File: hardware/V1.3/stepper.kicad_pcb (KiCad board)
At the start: 4 copper layers, 40 x 40 mm, 119 parts, among them J101 USB-MINI-B-SMD, J102 DRILL, J103 DRILL, J104 DRILL, J105 DRILL, J401 STACK-UP-HIGH, J402 STACK-DOWN, J403 STACK-UP-HIGH, J404 STACK-DOWN, P201 black, P202 green, P301 CON-SENSOR, P302 CON-SENSOR, Q201 FDS8449, Q202 AO4421, Q203 2N7002, SW101 Reset, SW102 Erase, U101 AT91SAM3SXB, U102 82400152, U201 ZXCT1086, U202 TMC21XX, U501 LD1117, X101 16Mhz

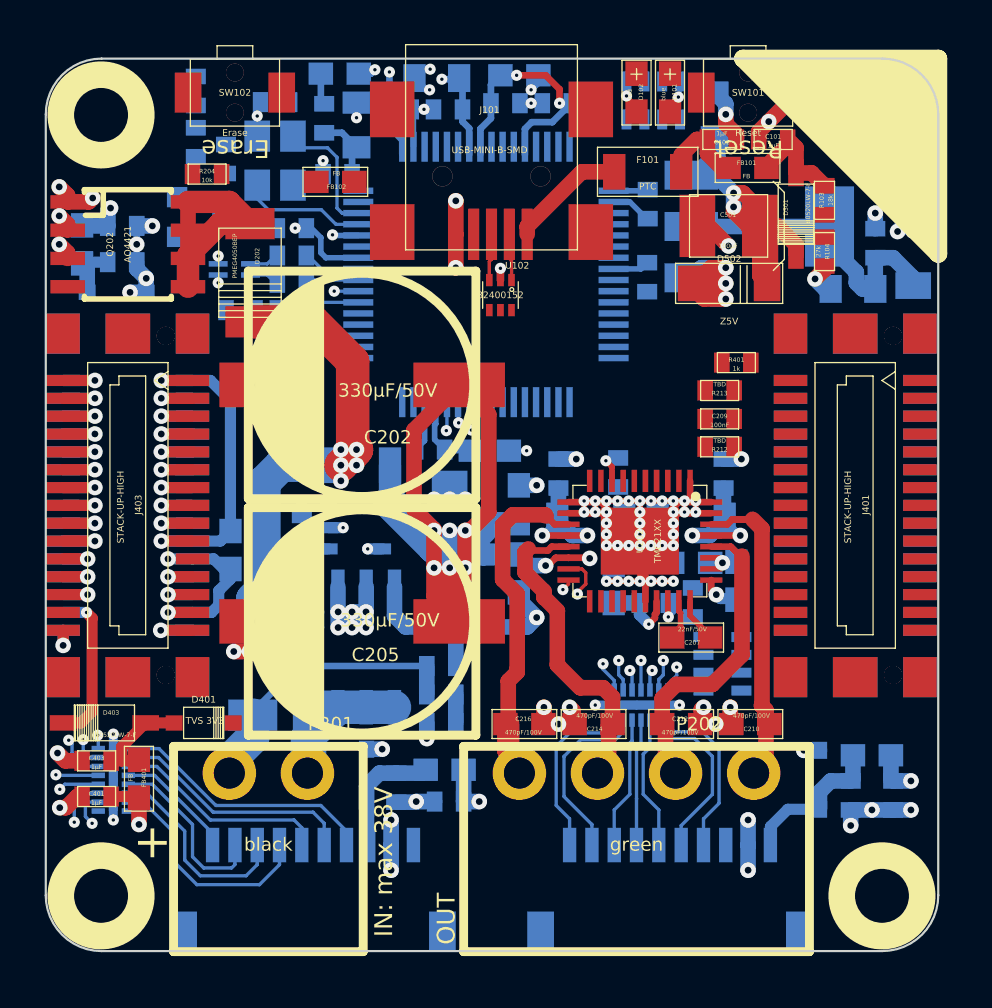
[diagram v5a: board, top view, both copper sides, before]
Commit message: routable, no drc errors
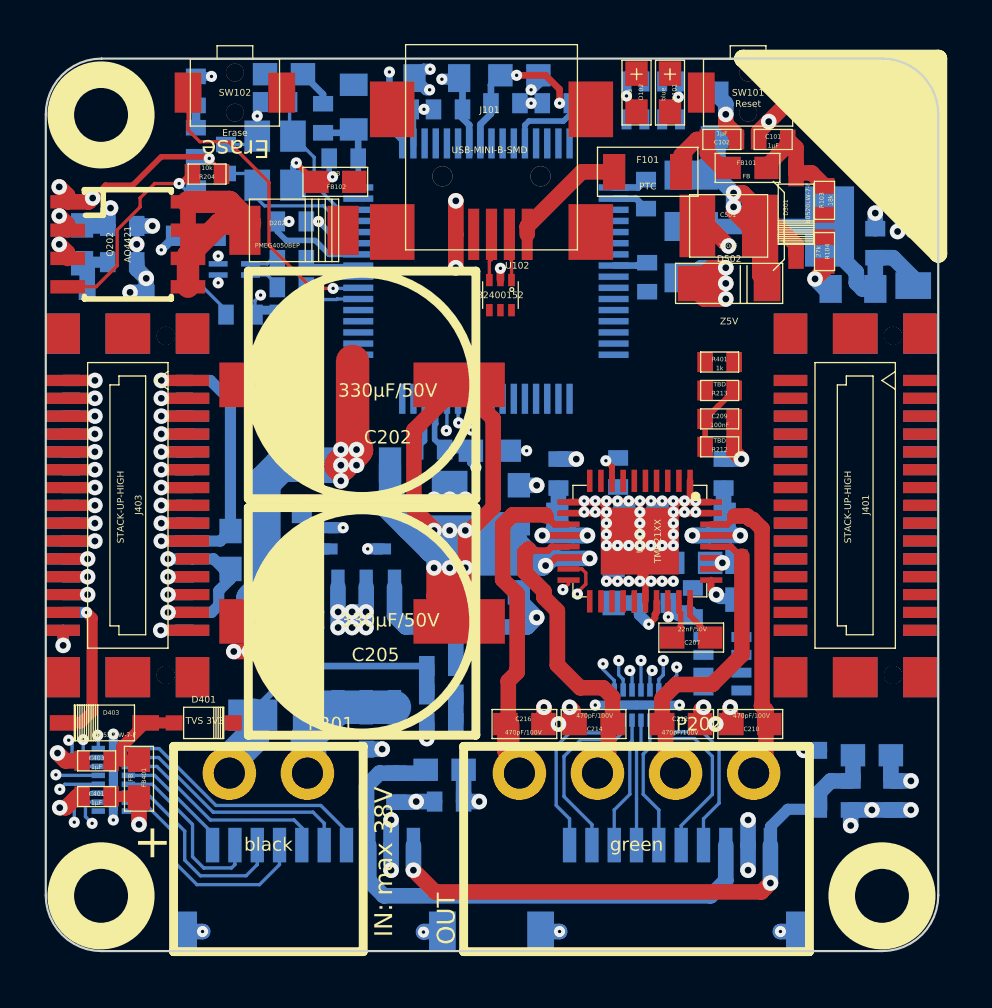
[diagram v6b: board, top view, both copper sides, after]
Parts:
- moved D202 2.74 mm to (137.8, 80.5), turned to 180 degrees
- moved C516 2.50 mm to (137.4, 73.5), turned to 180 degrees
- moved L501 0.81 mm to (140.5, 75.0)
- moved C517 0.75 mm to (140.1, 77.2)
- moved R401 0.75 mm to (156.9, 86.4)
- moved C506 0.46 mm to (153.6, 78.8)
- moved C508 0.30 mm to (137.8, 80.1), turned to 0 degrees
- moved Q203 0.25 mm to (133.4, 79.7), turned to 0 degrees
- moved C513 0.20 mm to (137.8, 84.2)
- moved R101 0.20 mm to (137.8, 83.0)
- moved R102 0.20 mm to (137.8, 81.8)
- moved R208 0.20 mm to (135.4, 84.2)
- moved U101 0.15 mm to (146.4, 82.3)
- turned R204 to 0 degrees
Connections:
- U101 pad 29: Net-(RP101-Pad5) -> Net-(RP101-Pad8)
- U101 pad 30: Net-(RP101-Pad8) -> Net-(RP101-Pad5)
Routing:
- net GND: track 84.6 -> 168.6 mm, vias 51 -> 57
- net Net-(C304-Pad1): track 5.64 -> 25.4 mm
- net Net-(C303-Pad1): track 6.92 -> 26.3 mm, vias 0 -> 2
- net VEE: track 58.5 -> 72.5 mm
- net Net-(SW102-Pad1): track 1.08 -> 13.9 mm
- net Net-(Q202-PadG): track 0.00 -> 9.74 mm, vias 0 -> 1
- net STACK-PVCC: track 32.1 -> 39.7 mm, vias 14 -> 15
- net Net-(D202-Pad2): track 25.7 -> 20.3 mm
- net PWR-VSTACK-SW: track 0.00 -> 4.30 mm
- net Net-(C209-Pad2): track 0.00 -> 3.08 mm
- net STACK-PGND: track 117.2 -> 120.1 mm, vias 77 -> 78
- net Net-(C218-Pad2): track 6.33 -> 8.48 mm
- net Net-(C217-Pad2): track 6.08 -> 8.11 mm
- net 3V3: track 40.5 -> 42.4 mm, vias 8 -> 9
- net XIN: track 5.69 -> 7.33 mm
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
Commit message: change power routing
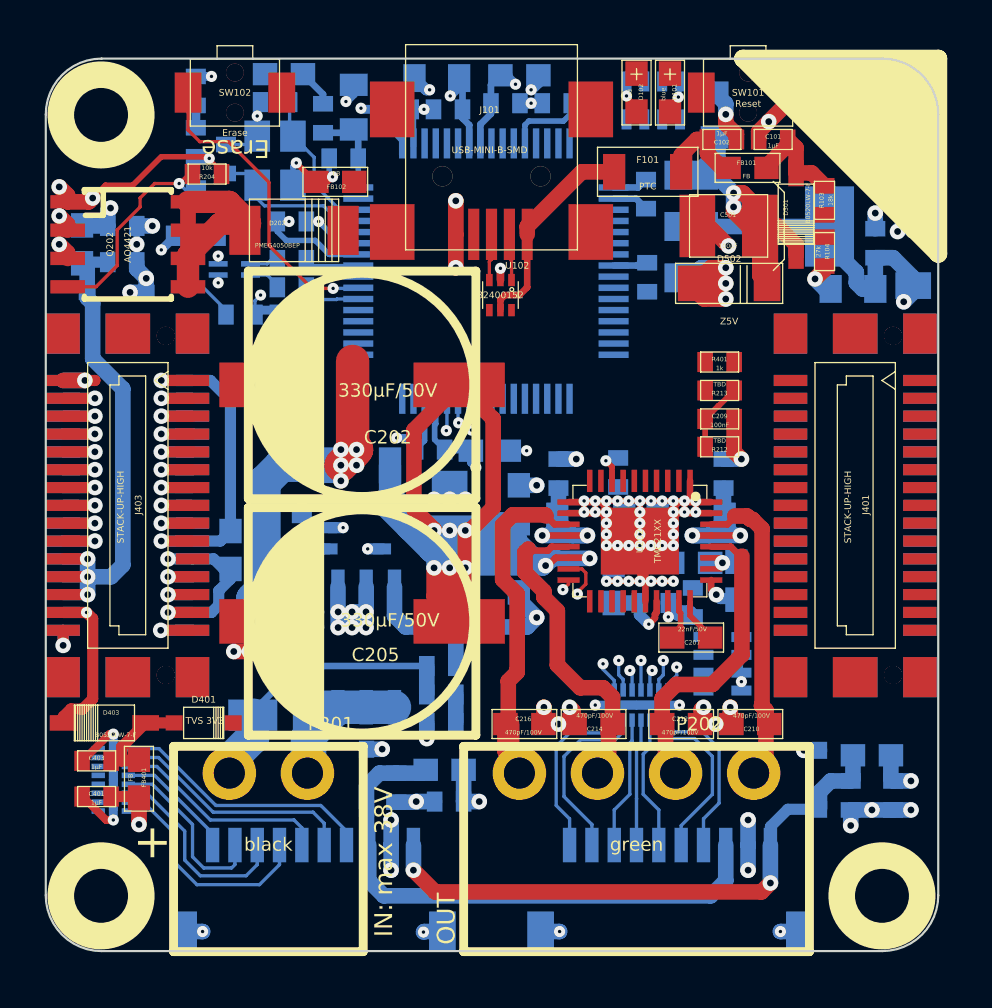
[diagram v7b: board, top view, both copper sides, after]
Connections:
- FILTER301 pad 14: 3V3 -> GND
- FILTER302 pad 14: GND -> 3V3
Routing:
- net VSTACK: track 20.9 -> 88.1 mm
- net STACK-PGND: track 120.1 -> 178.0 mm
- net STACK-PVCC: track 39.7 -> 74.2 mm
- net GND: track 168.6 -> 185.8 mm, vias 57 -> 54
- net Net-(C404-Pad1): track 9.01 -> 25.3 mm
- net Net-(F101-Pad2): track 5.26 -> 9.54 mm
- net BRICKLET-IO0_1: track 2.08 -> 0.00 mm, vias 1 -> 0
- net Net-(C509-Pad1): track 15.7 -> 13.8 mm
- net BRICKLET-IO0_3: track 1.91 -> 0.00 mm, vias 1 -> 0
- net BRICKLET-IO0_2/PWM0: track 1.82 -> 0.00 mm, vias 1 -> 0
- net BRICKLET-IO0_0/AD0: track 1.56 -> 0.00 mm, vias 1 -> 0
- net 3V3: track 42.4 -> 43.9 mm, vias 9 -> 11
- net BRICKLET-I2C-SDA: track 3.64 -> 2.35 mm, vias 3 -> 2
- net Net-(D403-Pad2): track 7.11 -> 8.02 mm
- net BRICKLET-I2C-SCL: track 1.80 -> 1.19 mm, vias 2 -> 1

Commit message: fix power diode position
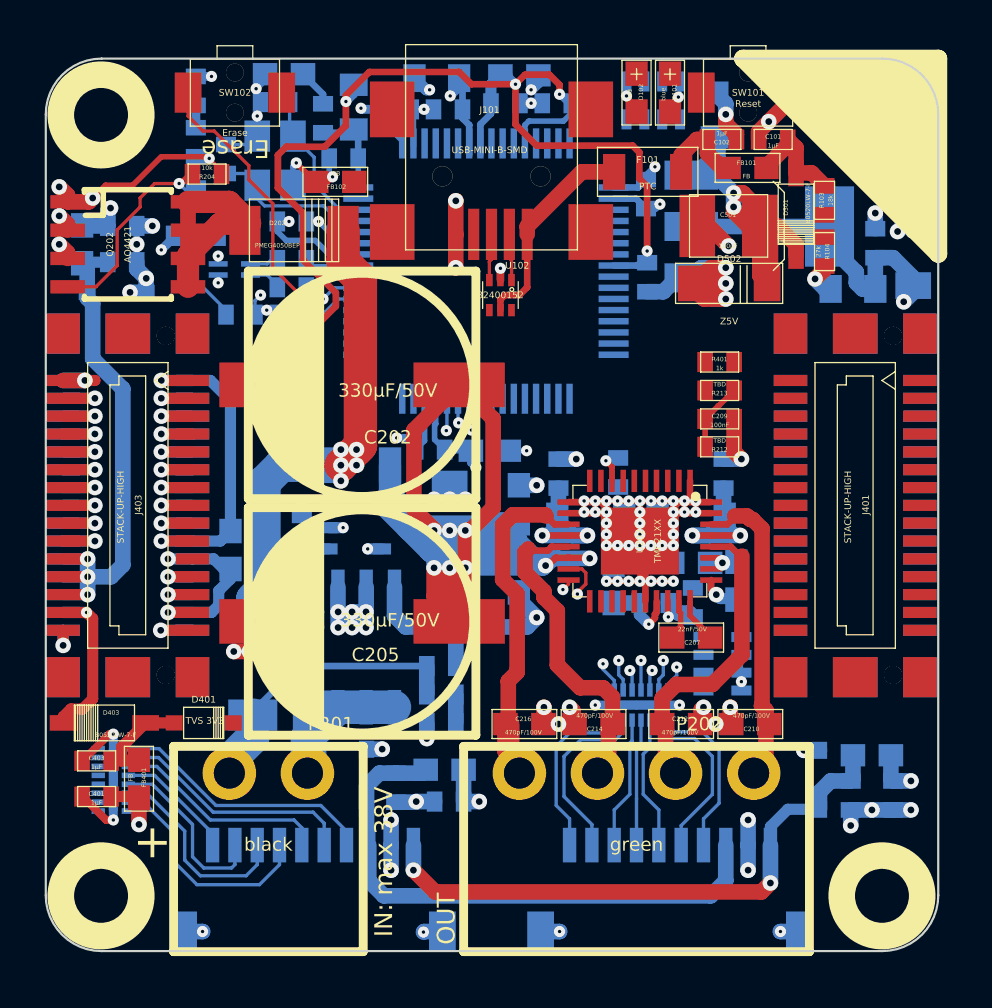
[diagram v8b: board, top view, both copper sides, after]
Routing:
- net Net-(C509-Pad1): track 13.8 -> 53.6 mm, vias 2 -> 5
- net Net-(D202-Pad2): track 20.3 -> 26.2 mm
- net GND: track 185.8 -> 189.6 mm, vias 54 -> 57
- net 3V3: track 43.9 -> 44.6 mm, vias 11 -> 12
